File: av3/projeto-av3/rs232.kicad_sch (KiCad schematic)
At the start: 9 parts, among them J6 DE9_Plug, U6 MAX232

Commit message: Esquemático finalizado, faltando somente o PCB.
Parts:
- removed C8: C, symbol Device:C
- C3, C4, C5, C6: value C_Polarized -> 1uF; footprint (none) -> Capacitor_SMD:CP_Elec_3x5.3
- C7: value C_Polarized -> 10uF/35V; footprint (none) -> Capacitor_SMD:CP_Elec_5x5.7
- C9: value C -> 100nF; footprint (none) -> Capacitor_SMD:C_1206_3216Metric
- J6: footprint (none) -> Connector_Dsub:DSUB-9_Female_Horizontal_P2.77x2.84mm_EdgePinOffset4.94mm_Housed_MountingHolesOffset7.48mm
- U6: footprint (none) -> Package_SO:SOIC-16_4.55x10.3mm_P1.27mm
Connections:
- net GND: now also C7.2, C9.2
- net at J6.2: now also U6.13 (R1IN)
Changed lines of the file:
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@@
+	(wire
+		(pts
+			(xy 138.43 96.52) (xy 138.43 97.79)
+		)
+		(stroke
+			(width 0)
+			(type default)
+		)
+	)
 	(wire
 		(pts
@@
 	(wire
 		(pts
-			(xy 124.46 97.79) (xy 157.48 97.79)
+			(xy 138.43 97.79) (xy 124.46 97.79)
 		)
 		(stroke
@@
 	(wire
 		(pts
-			(xy 138.43 91.44) (xy 157.48 91.44)
+			(xy 138.43 96.52) (xy 157.48 96.52)
 		)
 		(stroke
@@
 	(wire
 		(pts
-			(xy 104.14 46.99) (xy 104.14 54.61)
+			(xy 138.43 91.44) (xy 157.48 91.44)
 		)
 		(stroke
@@
 		)
 	)
+	(wire
+		(pts
+			(xy 104.14 46.99) (xy 104.14 54.61)
+		)
+		(stroke
+			(width 0)
+			(type default)
+		)
+	)
 	(global_label "RX"
 		(shape input)
@@
 		(on_board yes)
 		(dnp no)
-		(fields_autoplaced yes)
 		(property "Reference" "C6"
-			(at 87.63 63.8809 0)
+			(at 82.296 57.658 0)
 			(effects
 				(font
@@
 			)
 		)
-		(property "Value" "C_Polarized"
-			(at 87.63 66.4209 0)
+		(property "Value" "1uF"
+			(at 82.296 60.198 0)
 			(effects
 				(font
@@
 			)
 		)
-		(property "Footprint" ""
+		(property "Footprint" "Capacitor_SMD:CP_Elec_3x5.3"
 			(at 84.7852 69.85 0)
 			(effects
@@
 	)
 	(symbol
+		(lib_id "power:GND")
+		(at 111.76 46.99 90)
+		(unit 1)
+		(exclude_from_sim no)
+		(in_bom yes)
+		(on_board yes)
+		(dnp no)
+		(fields_autoplaced yes)
+		(property "Reference" "#PWR067"
+			(at 118.11 46.99 0)
+			(effects
+				(font
+					(size 1.27 1.27)
+				)
+				(hide yes)
+			)
+		)
+		(property "Value" "GND"
+			(at 115.57 46.9899 90)
+			(effects
+				(font
+					(size 1.27 1.27)
+				)
+				(justify right)
+			)
+		)
+		(property "Footprint" ""
+			(at 111.76 46.99 0)
+			(effects
+				(font
+					(size 1.27 1.27)
+				)
+				(hide yes)
+			)
+		)
+		(property "Datasheet" ""
+			(at 111.76 46.99 0)
+			(effects
+				(font
+					(size 1.27 1.27)
+				)
+				(hide yes)
+			)
+		)
+		(property "Description" "Power symbol creates a global label with name \"GND\" , ground"
+			(at 111.76 46.99 0)
+			(effects
+				(font
+					(size 1.27 1.27)
+				)
+				(hide yes)
+			)
+		)
+		(pin "1"
+		)
+		(instances
+			(project "av3"
+				(path "/82998b71-606c-4e03-99b7-477e2a65cb94/99ed4151-0889-4591-936c-afdf281a07a2"
+					(reference "#PWR067")
+					(unit 1)
+				)
+			)
+		)
+	)
+	(symbol
 		(lib_id "power:+5V")
 		(at 104.14 46.99 90)
@@
 			)
 		)
-		(property "Value" "C_Polarized"
+		(property "Value" "1uF"
 			(at 127.381 69.85 90)
 			(effects
@@
 			)
 		)
-		(property "Footprint" ""
+		(property "Footprint" "Capacitor_SMD:CP_Elec_3x5.3"
 			(at 132.08 73.9648 0)
 			(effects
@@
 	)
 	(symbol
+		(lib_id "power:GND")
+		(at 111.76 54.61 90)
+		(unit 1)
+		(exclude_from_sim no)
+		(in_bom yes)
+		(on_board yes)
+		(dnp no)
+		(fields_autoplaced yes)
+		(property "Reference" "#PWR068"
+			(at 118.11 54.61 0)
+			(effects
+				(font
+					(size 1.27 1.27)
+				)
+				(hide yes)
+			)
+		)
+		(property "Value" "GND"
+			(at 115.57 54.6099 90)
+			(effects
+				(font
+					(size 1.27 1.27)
+				)
+				(justify right)
+			)
+		)
+		(property "Footprint" ""
+			(at 111.76 54.61 0)
+			(effects
+				(font
+					(size 1.27 1.27)
+				)
+				(hide yes)
+			)
+		)
+		(property "Datasheet" ""
+			(at 111.76 54.61 0)
+			(effects
+				(font
+					(size 1.27 1.27)
+				)
+				(hide yes)
+			)
+		)
+		(property "Description" "Power symbol creates a global label with name \"GND\" , ground"
+			(at 111.76 54.61 0)
+			(effects
+				(font
+					(size 1.27 1.27)
+				)
+				(hide yes)
+			)
+		)
+		(pin "1"
+		)
+		(instances
+			(project "av3"
+				(path "/82998b71-606c-4e03-99b7-477e2a65cb94/99ed4151-0889-4591-936c-afdf281a07a2"
+					(reference "#PWR068")
+					(unit 1)
+				)
+			)
+		)
+	)
+	(symbol
 		(lib_id "Connector:DE9_Plug")
 		(at 165.1 91.44 0)
@@
 			)
 		)
-		(property "Footprint" ""
+		(property "Footprint" "Connector_Dsub:DSUB-9_Female_Horizontal_P2.77x2.84mm_EdgePinOffset4.94mm_Housed_MountingHolesOffset7.48mm"
 			(at 165.1 91.44 0)
 			(effects
@@
 		(on_board yes)
 		(dnp no)
-		(fields_autoplaced yes)
 		(property "Reference" "C3"
-			(at 128.27 63.8809 0)
+			(at 123.444 58.42 0)
 			(effects
 				(font
@@
 			)
 		)
-		(property "Value" "C_Polarized"
-			(at 128.27 66.4209 0)
+		(property "Value" "1uF"
+			(at 123.444 60.96 0)
 			(effects
 				(font
@@
 			)
 		)
-		(property "Footprint" ""
+		(property "Footprint" "Capacitor_SMD:CP_Elec_3x5.3"
 			(at 125.4252 69.85 0)
 			(effects
@@
 			)
 		)
-		(property "Value" "C_Polarized"
+		(property "Value" "1uF"
 			(at 129.159 77.47 90)
 			(effects
@@
 			)
 		)
-		(property "Footprint" ""
+		(property "Footprint" "Capacitor_SMD:CP_Elec_3x5.3"
 			(at 124.46 83.5152 0)
 			(effects
@@
 	)
 	(symbol
-		(lib_id "Device:C")
-		(at 127 53.34 90)
-		(unit 1)
-		(exclude_from_sim no)
-		(in_bom yes)
-		(on_board yes)
-		(dnp no)
-		(fields_autoplaced yes)
-		(property "Reference" "C8"
-			(at 127 45.72 90)
-			(effects
-				(font
-					(size 1.27 1.27)
-				)
-			)
-		)
-		(property "Value" "C"
-			(at 127 48.26 90)
-			(effects
-				(font
-					(size 1.27 1.27)
-				)
-			)
-		)
-		(property "Footprint" ""
-			(at 130.81 52.3748 0)
-			(effects
-				(font
-					(size 1.27 1.27)
-				)
-				(hide yes)
-			)
-		)
-		(property "Datasheet" "~"
-			(at 127 53.34 0)
-			(effects
-				(font
-					(size 1.27 1.27)
-				)
-				(hide yes)
-			)
-		)
-		(property "Description" "Unpolarized capacitor"
-			(at 127 53.34 0)
-			(effects
-				(font
-					(size 1.27 1.27)
-				)
-				(hide yes)
-			)
-		)
-		(pin "1"
-		)
-		(pin "2"
-		)
-		(instances
-			(project "av3"
-				(path "/82998b71-606c-4e03-99b7-477e2a65cb94/99ed4151-0889-4591-936c-afdf281a07a2"
-					(reference "C8")
-					(unit 1)
-				)
-			)
-		)
-	)
-	(symbol
 		(lib_id "Device:C_Polarized")
 		(at 107.95 46.99 90)
@@
 			)
 		)
-		(property "Value" "C_Polarized"
+		(property "Value" "10uF/35V"
 			(at 107.061 41.91 90)
 			(effects
@@
 			)
 		)
-		(property "Footprint" ""
+		(property "Footprint" "Capacitor_SMD:CP_Elec_5x5.7"
 			(at 111.76 46.0248 0)
 			(effects
@@
 		(dnp no)
 		(property "Reference" "U6"
-			(at 113.03 55.118 0)
+			(at 93.98 55.118 0)
 			(effects
 				(font
@@
 		)
 		(property "Value" "MAX232"
-			(at 113.03 57.658 0)
+			(at 93.98 57.658 0)
 			(effects
 				(font
@@
 			)
 		)
-		(property "Footprint" ""
+		(property "Footprint" "Package_SO:SOIC-16_4.55x10.3mm_P1.27mm"
 			(at 105.41 111.76 0)
 			(effects
@@
 			)
 		)
-		(property "Value" "C"
+		(property "Value" "100nF"
 			(at 107.95 49.53 90)
 			(effects
@@
 			)
 		)
-		(property "Footprint" ""
+		(property "Footprint" "Capacitor_SMD:C_1206_3216Metric"
 			(at 111.76 53.6448 0)
 			(effects

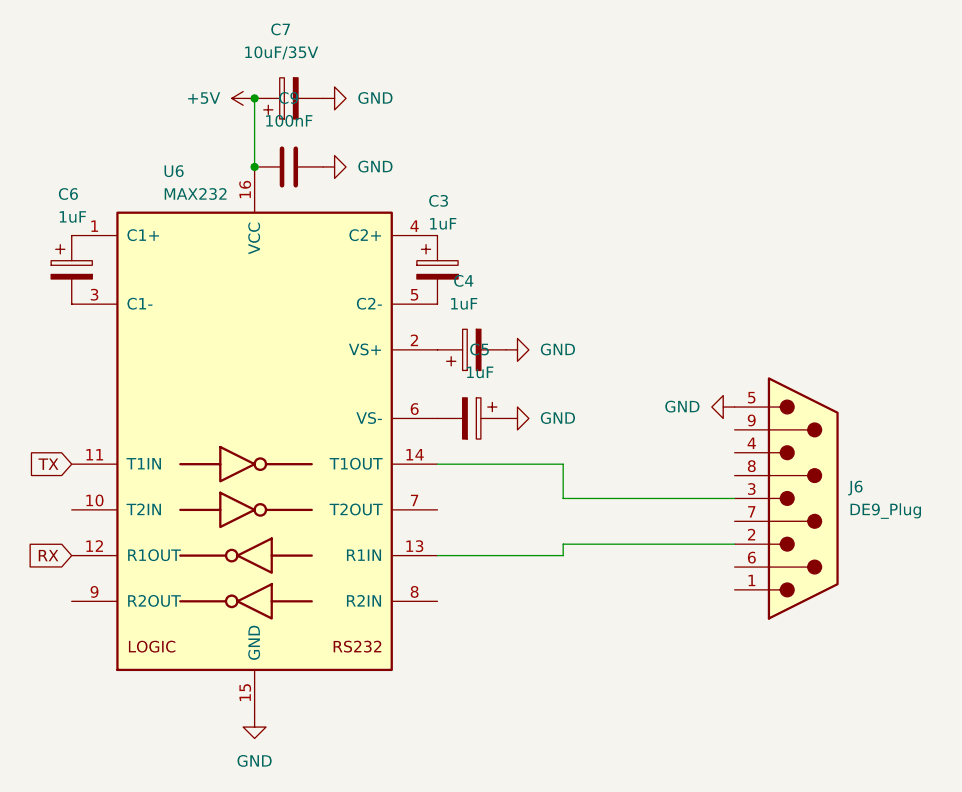
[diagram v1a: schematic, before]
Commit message: Referencias de componentes resetados; Progresso de 20% no PCB;
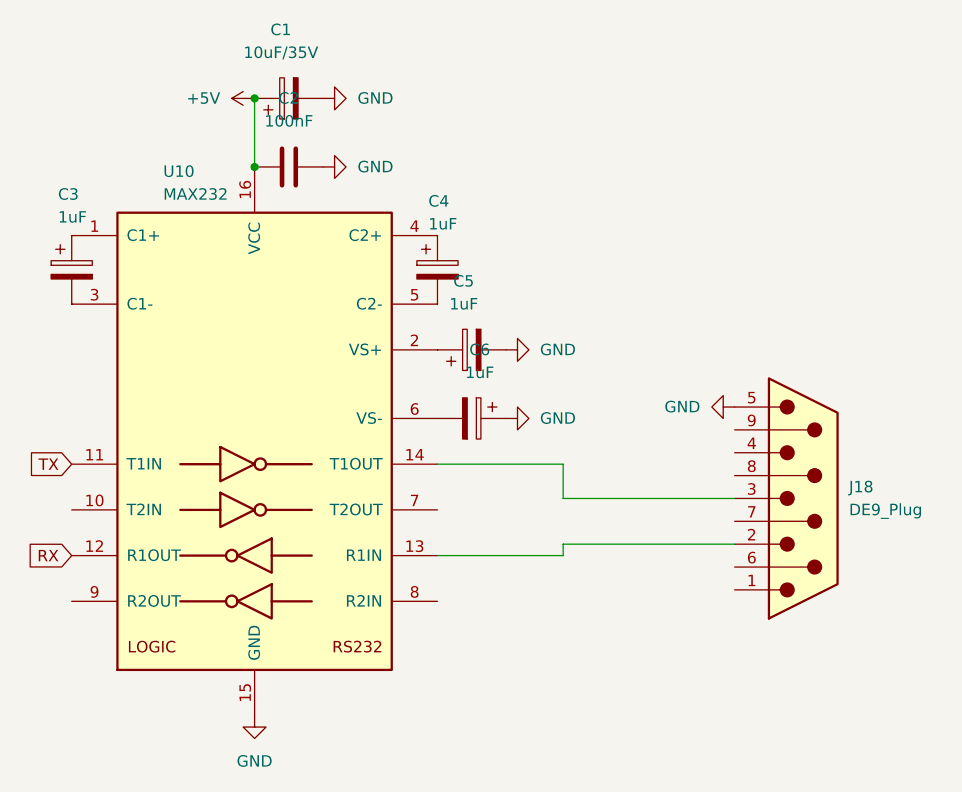
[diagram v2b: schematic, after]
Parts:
- renumbered C7 to C1, C9 to C2, C6 to C3, C3 to C4, C4 to C5, C5 to C6, J6 to J18, U6 to U10
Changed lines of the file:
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@@
 		(on_board yes)
 		(dnp no)
-		(property "Reference" "C6"
+		(property "Reference" "C3"
 			(at 82.296 57.658 0)
 			(effects
@@
 			(project "av3"
 				(path "/82998b71-606c-4e03-99b7-477e2a65cb94/99ed4151-0889-4591-936c-afdf281a07a2"
-					(reference "C6")
+					(reference "C3")
 					(unit 1)
 				)
@@
 		(dnp no)
 		(fields_autoplaced yes)
-		(property "Reference" "#PWR055"
+		(property "Reference" "#PWR067"
 			(at 104.14 121.92 0)
 			(effects
@@
 			(project "av3"
 				(path "/82998b71-606c-4e03-99b7-477e2a65cb94/99ed4151-0889-4591-936c-afdf281a07a2"
-					(reference "#PWR055")
+					(reference "#PWR067")
 					(unit 1)
 				)
@@
 		(dnp no)
 		(fields_autoplaced yes)
-		(property "Reference" "#PWR067"
+		(property "Reference" "#PWR062"
 			(at 118.11 46.99 0)
 			(effects
@@
 			(project "av3"
 				(path "/82998b71-606c-4e03-99b7-477e2a65cb94/99ed4151-0889-4591-936c-afdf281a07a2"
-					(reference "#PWR067")
+					(reference "#PWR062")
 					(unit 1)
 				)
@@
 		(dnp no)
 		(fields_autoplaced yes)
-		(property "Reference" "#PWR054"
+		(property "Reference" "#PWR061"
 			(at 107.95 46.99 0)
 			(effects
@@
 			(project "av3"
 				(path "/82998b71-606c-4e03-99b7-477e2a65cb94/99ed4151-0889-4591-936c-afdf281a07a2"
-					(reference "#PWR054")
+					(reference "#PWR061")
 					(unit 1)
 				)
@@
 		(dnp no)
 		(fields_autoplaced yes)
-		(property "Reference" "C4"
+		(property "Reference" "C5"
 			(at 127.381 67.31 90)
 			(effects
@@
 			(project "av3"
 				(path "/82998b71-606c-4e03-99b7-477e2a65cb94/99ed4151-0889-4591-936c-afdf281a07a2"
-					(reference "C4")
+					(reference "C5")
 					(unit 1)
 				)
@@
 		(dnp no)
 		(fields_autoplaced yes)
-		(property "Reference" "#PWR052"
+		(property "Reference" "#PWR064"
 			(at 138.43 74.93 0)
 			(effects
@@
 			(project "av3"
 				(path "/82998b71-606c-4e03-99b7-477e2a65cb94/99ed4151-0889-4591-936c-afdf281a07a2"
-					(reference "#PWR052")
+					(reference "#PWR064")
 					(unit 1)
 				)
@@
 		(dnp no)
 		(fields_autoplaced yes)
-		(property "Reference" "#PWR068"
+		(property "Reference" "#PWR063"
 			(at 118.11 54.61 0)
 			(effects
@@
 			(project "av3"
 				(path "/82998b71-606c-4e03-99b7-477e2a65cb94/99ed4151-0889-4591-936c-afdf281a07a2"
-					(reference "#PWR068")
+					(reference "#PWR063")
 					(unit 1)
 				)
@@
 		(dnp no)
 		(fields_autoplaced yes)
-		(property "Reference" "J6"
+		(property "Reference" "J18"
 			(at 170.18 90.1699 0)
 			(effects
@@
 			(project "av3"
 				(path "/82998b71-606c-4e03-99b7-477e2a65cb94/99ed4151-0889-4591-936c-afdf281a07a2"
-					(reference "J6")
+					(reference "J18")
 					(unit 1)
 				)
@@
 		(on_board yes)
 		(dnp no)
-		(property "Reference" "C3"
+		(property "Reference" "C4"
 			(at 123.444 58.42 0)
 			(effects
@@
 			(project "av3"
 				(path "/82998b71-606c-4e03-99b7-477e2a65cb94/99ed4151-0889-4591-936c-afdf281a07a2"
-					(reference "C3")
+					(reference "C4")
 					(unit 1)
 				)
@@
 		(dnp no)
 		(fields_autoplaced yes)
-		(property "Reference" "C5"
+		(property "Reference" "C6"
 			(at 129.159 74.93 90)
 			(effects
@@
 			(project "av3"
 				(path "/82998b71-606c-4e03-99b7-477e2a65cb94/99ed4151-0889-4591-936c-afdf281a07a2"
-					(reference "C5")
+					(reference "C6")
 					(unit 1)
 				)
@@
 		(dnp no)
 		(fields_autoplaced yes)
-		(property "Reference" "C7"
+		(property "Reference" "C1"
 			(at 107.061 39.37 90)
 			(effects
@@
 			(project "av3"
 				(path "/82998b71-606c-4e03-99b7-477e2a65cb94/99ed4151-0889-4591-936c-afdf281a07a2"
-					(reference "C7")
+					(reference "C1")
 					(unit 1)
 				)
@@
 		(on_board yes)
 		(dnp no)
-		(property "Reference" "U6"
+		(property "Reference" "U10"
 			(at 93.98 55.118 0)
 			(effects
@@
 			(project "av3"
 				(path "/82998b71-606c-4e03-99b7-477e2a65cb94/99ed4151-0889-4591-936c-afdf281a07a2"
-					(reference "U6")
+					(reference "U10")
 					(unit 1)
 				)
@@
 		(on_board yes)
 		(dnp no)
-		(property "Reference" "C9"
+		(property "Reference" "C2"
 			(at 107.95 46.99 90)
 			(effects
@@
 			(project "av3"
 				(path "/82998b71-606c-4e03-99b7-477e2a65cb94/99ed4151-0889-4591-936c-afdf281a07a2"
-					(reference "C9")
+					(reference "C2")
 					(unit 1)
 				)
@@
 		(dnp no)
 		(fields_autoplaced yes)
-		(property "Reference" "#PWR051"
+		(property "Reference" "#PWR065"
 			(at 151.13 81.28 0)
 			(effects
@@
 			(project "av3"
 				(path "/82998b71-606c-4e03-99b7-477e2a65cb94/99ed4151-0889-4591-936c-afdf281a07a2"
-					(reference "#PWR051")
+					(reference "#PWR065")
 					(unit 1)
 				)
@@
 		(dnp no)
 		(fields_autoplaced yes)
-		(property "Reference" "#PWR053"
+		(property "Reference" "#PWR066"
 			(at 138.43 82.55 0)
 			(effects
@@
 			(project "av3"
 				(path "/82998b71-606c-4e03-99b7-477e2a65cb94/99ed4151-0889-4591-936c-afdf281a07a2"
-					(reference "#PWR053")
-					(unit 1)
-				)
+					(reference "#PWR066")
+					(unit 1)
+				)
